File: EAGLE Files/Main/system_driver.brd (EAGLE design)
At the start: 59.4 x 64.8 mm, 12 parts

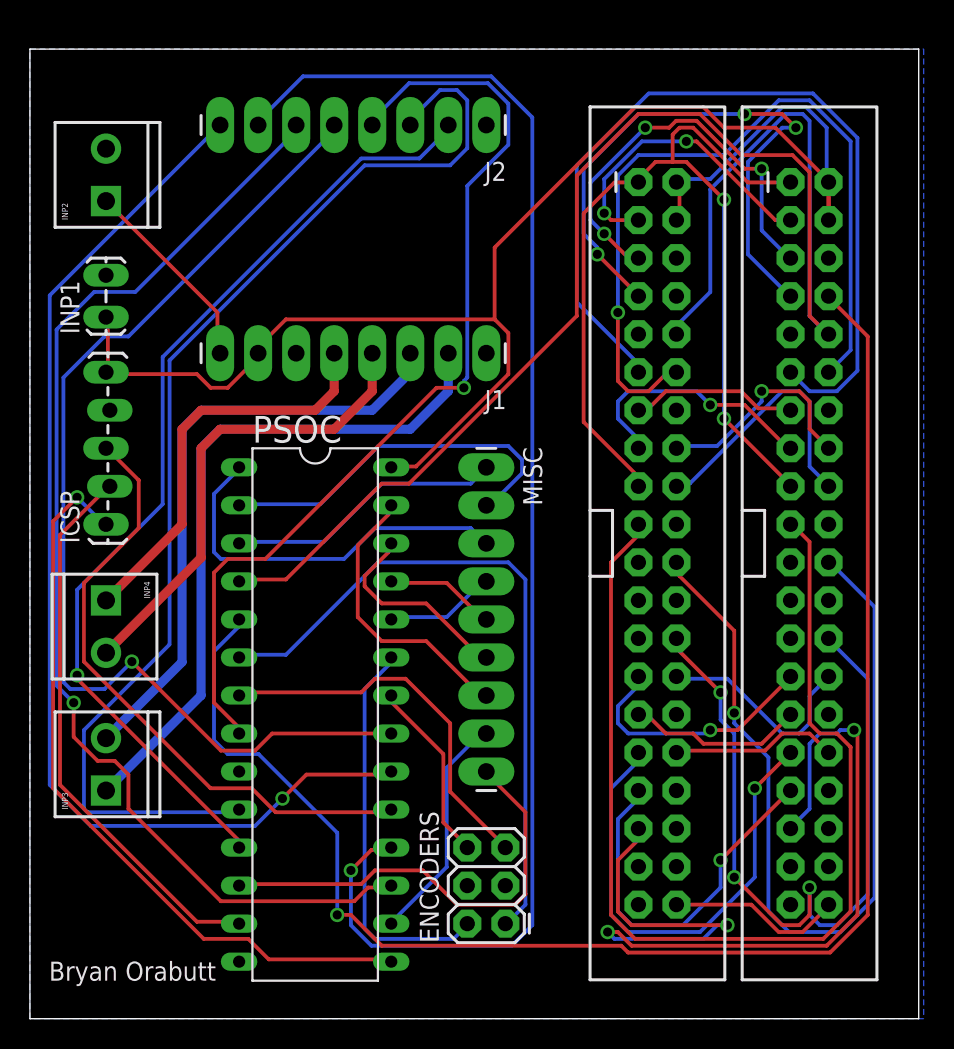
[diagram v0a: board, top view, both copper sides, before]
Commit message: updated EAGLE files
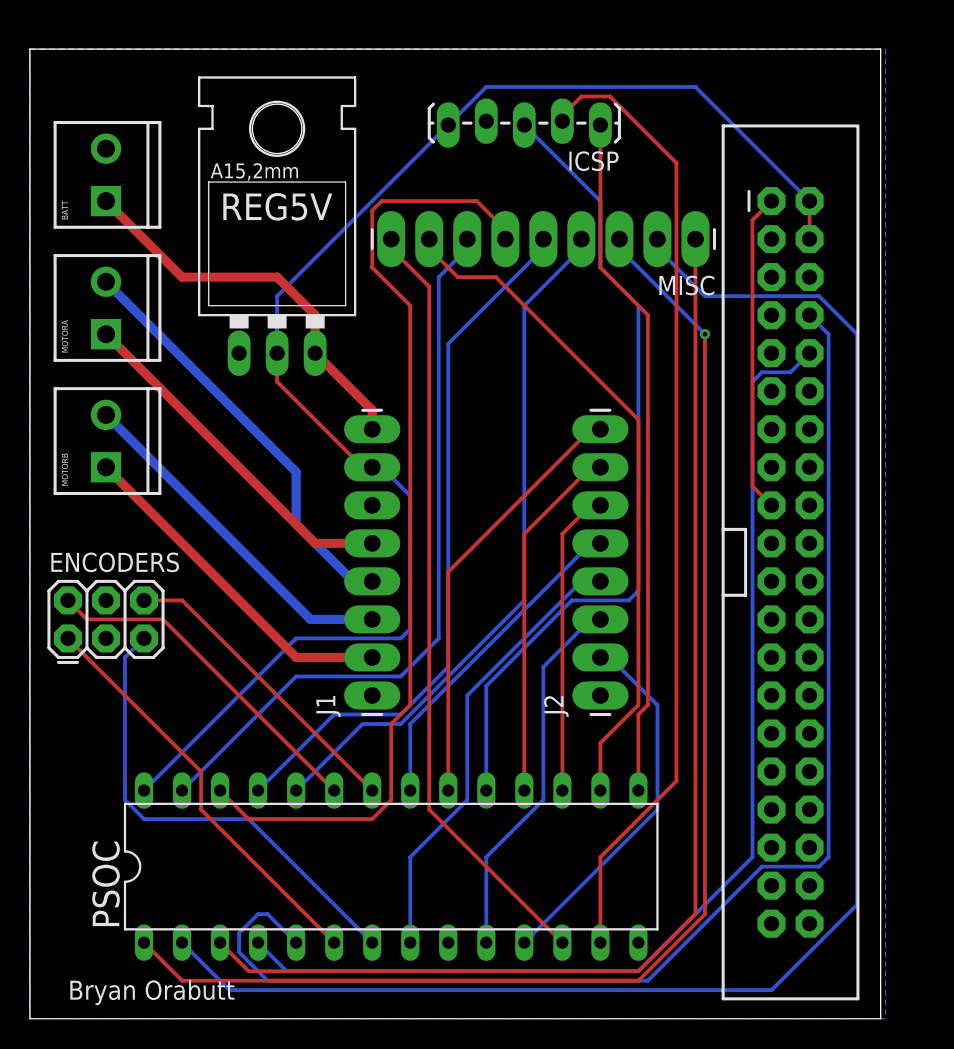
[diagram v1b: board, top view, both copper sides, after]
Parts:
- removed INP1: (no value), SparkFun-Connectors:1X02_LOCK_LONGPADS
- removed INP3, INP4: (no value), SparkFun-Connectors:SCREWTERMINAL-3.5MM-2
- removed PI1: RASPBERRYPI-40-PIN-GPIO, SparkFun-Boards:2X20-SHROUDED
- added MOTORA, MOTORB: (no value), SparkFun-Connectors:SCREWTERMINAL-3.5MM-2
- added REG5V: L7805, SparkFun-PowerIC:78XXL
- ENCODERS: value FEMALE 2x3 -> (none)
- moved ICSP 42.4 mm to (43.2, 74.9), turned to 180 degrees
- moved J2 38.9 mm to (43.2, 36.8), turned to 90 degrees
- moved ENCODERS 34.9 mm to (7.62, 40.6), turned to 0 degrees
- moved J1 24.1 mm to (27.9, 36.8), turned to 90 degrees
- moved MISC 20.7 mm to (49.5, 67.3), turned to 180 degrees
- moved PSOC 11.4 mm to (29.2, 25.4), turned to 0 degrees
- moved PI 8.98 mm to (55.9, 45.7)
- renumbered INP2 to BATT
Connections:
- net 3.3V: no longer PI1.1, PI1.17
- net AO1: now also MOTORA.1; no longer INP4.1
- net AO2: now also MOTORA.2; no longer INP4.2
- net BO1: now also MOTORB.1; no longer INP3.1
- net BO2: now also MOTORB.2; no longer INP3.2
- net CE0: no longer PI1.24
- net CE1: no longer PI1.26
- net GND: now also REG5V.IN; no longer INP1.2, PI1.14, PI1.20, PI1.25, PI1.30, PI1.34, PI1.39, PI1.6, PI1.9
- net GP12: no longer PI1.32
- net GP13: no longer PI1.33
- net GP16: no longer PI1.36
- net GP17: no longer PI1.11
- net GP18: no longer PI1.12
- net GP19: no longer PI1.35
- net GP20: no longer PI1.38
- net GP21: no longer PI1.40
- net GP22: no longer PI1.15
- net GP23: no longer PI1.16
- net GP24: no longer PI1.18
- net GP25: no longer PI1.22
- net GP26: no longer PI1.37
- net GP27: no longer PI1.13
- net GP4: no longer PI1.7
- net GP5: no longer PI1.29
- net GP6: no longer PI1.31
- net ID_SC: no longer PI1.28
- net ID_SD: no longer PI1.27
- net MISO: no longer PI1.21
- net MOSI: no longer PI1.19
- net PI_SCL: no longer PI1.5
- net PI_SDA: no longer PI1.3
- net RX: no longer PI1.8
- net SCLK: no longer PI1.23
- net TX: no longer PI1.10
- net V+: now also REG5V.OUT
- net VCC: now also REG5V.GND; no longer INP1.1, PI1.2, PI1.4
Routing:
- net MISC1: track 25.2 -> 103.2 mm
- net MOSI: track 72.5 -> 0.00 mm
- net AIN2: track 95.4 -> 24.1 mm, vias 1 -> 0
- net GP19: track 62.3 -> 0.00 mm, vias 3 -> 0
- net MISC2: track 26.0 -> 87.8 mm, vias 0 -> 1
- net MISC0: track 18.6 -> 79.2 mm
- net GP17: track 58.6 -> 0.00 mm
- net GP25: track 58.3 -> 0.00 mm, vias 1 -> 0
- net AIN1: track 77.1 -> 20.5 mm, vias 1 -> 0
- net GP18: track 53.3 -> 0.00 mm, vias 1 -> 0
- net BIN2: track 77.2 -> 25.1 mm
- net CE1: track 51.0 -> 0.00 mm, vias 3 -> 0
- net MISC5: track 13.7 -> 64.3 mm
- net STDBY: track 71.6 -> 22.1 mm, vias 1 -> 0
- net PWMA: track 74.2 -> 28.7 mm, vias 1 -> 0
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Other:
- board size 59.4 x 64.8 mm -> 56.8 x 64.8 mm

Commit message: Updated PCB files, added PSoC code
Up to date PCB and schematic files for Robot 2's driver control board.
Also added the PSoC code files and project.
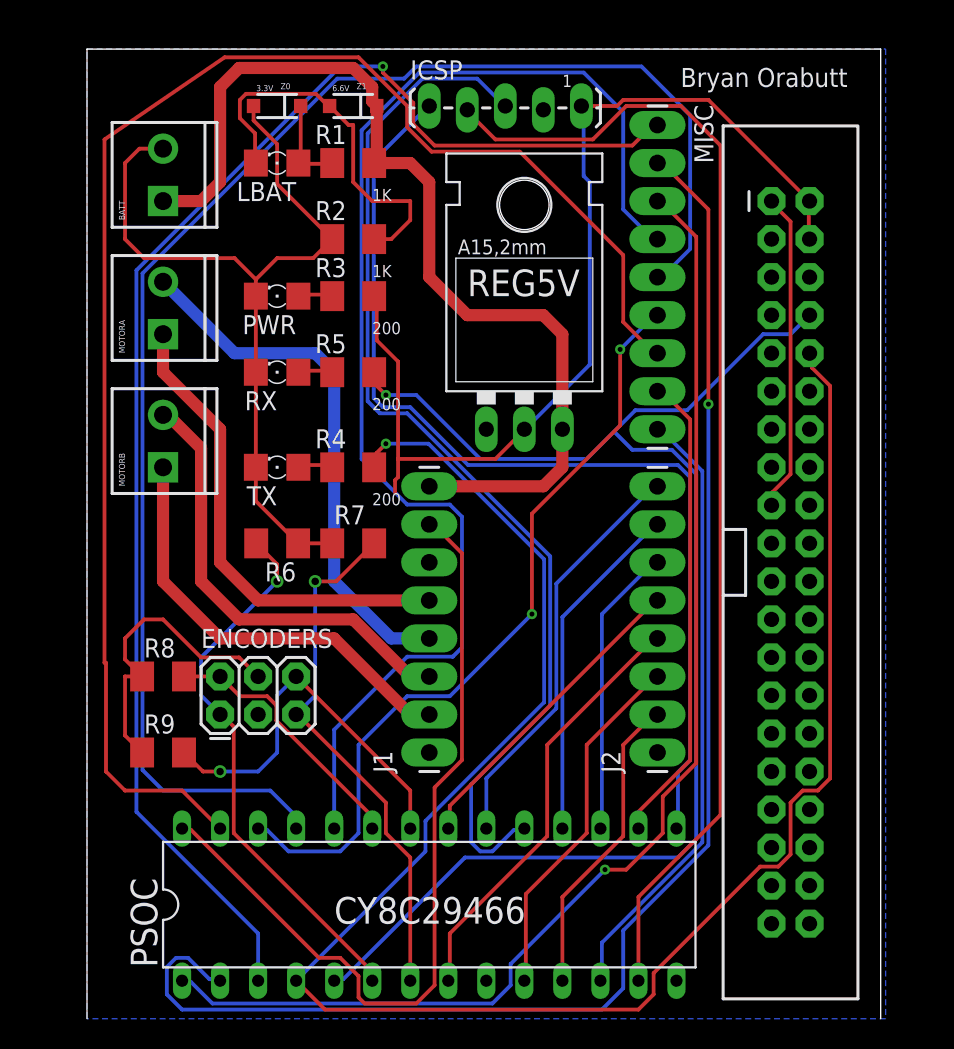
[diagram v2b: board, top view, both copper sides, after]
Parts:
- added LBAT, PWR, RX, TX: (no value), SparkFun-LED:FKIT-LED-1206
- added R1, R2: 1K, resistor:M1206
- added R3, R4, R5: 200, resistor:M1206
- added R6, R7, R8, R9: 10K, resistor:M1206
- added Z0: 3.3V, SparkFun-DiscreteSemi:SOD-123
- added Z1: 6.6V, SparkFun-DiscreteSemi:SOD-123
- moved REG5V 17.3 mm to (38.1, 58.4)
- moved ICSP 11.5 mm to (31.8, 76.2), turned to 0 degrees
- moved ENCODERS 11.4 mm to (17.8, 35.6)
- moved MISC 8.03 mm to (47.0, 74.9), turned to 270 degrees
- moved J2 5.39 mm to (47.0, 33.0)
- moved J1 5.39 mm to (31.8, 33.0)
- moved BATT 3.81 mm to (14.0, 69.8)
- moved MOTORA 3.81 mm to (14.0, 61.0)
- moved MOTORB 3.81 mm to (14.0, 52.1)
- moved PSOC 3.59 mm to (31.8, 22.9)
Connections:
- new net N$1: LBAT.A, R1.1, Z0.C
- new net N$2: LBAT.C, R2.2, Z1.A
- new net N$3: PWR.A, R3.1
- new net N$4: R4.1, TX.A
- new net N$5: R5.1, RX.A
- net ENC1A: now also R8.2
- net ENC1B: now also R9.2
- net ENC2A: now also R6.2
- net ENC2B: now also R7.2
- net GND: now also PSOC.9, PWR.C, R2.1, R6.1, R7.1, R8.1, R9.1, RX.C, TX.C, Z0.A
- net RX: now also R5.2
- net TX: now also R4.2
- net V+: now also R1.2, Z1.C
- net VCC: now also R3.2
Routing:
- net GND: track 0.00 -> 76.9 mm
- net MISC4: track 47.3 -> 101.2 mm
- net MISC6: track 48.8 -> 102.0 mm
- net TX: track 73.3 -> 125.4 mm, vias 0 -> 1
- net V+: track 26.3 -> 66.5 mm
- net MISC3: track 46.2 -> 86.2 mm
- net VCC: track 95.9 -> 123.5 mm
- net N$2: track 0.00 -> 25.6 mm
- net PSDA: track 46.0 -> 68.2 mm
- net XRES: track 54.0 -> 71.6 mm
- net MISC0: track 79.2 -> 95.1 mm, vias 0 -> 1
- net PSCK: track 64.5 -> 77.9 mm
- net MISC7: track 45.2 -> 31.9 mm
- net MISC5: track 64.3 -> 52.7 mm, vias 0 -> 2
- net MISC8: track 51.7 -> 41.0 mm
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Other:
- board size 56.8 x 64.8 mm -> 53 x 64.8 mm
- board text added: "1"
- board text added: "CY8C29466"
- board text added: "P00"
- board text added: "P02"
- board text added: "P03"
- board text added: "P04"
- board text added: "P05"
- board text added: "P06"
- board text added: "P07"
- board text added: "P12"
- board text added: "P13"

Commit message: fixed merge issues?
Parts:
- added PWR_SW: (no value), SparkFun-Electromechanical:SWITCH-SPDT
- moved Z0 1.27 mm to (21.6, 74.9)
- moved Z1 1.27 mm to (26.7, 74.9)
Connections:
- removed net MISO: PI.21
- removed net SCLK: PI.23
- new net REGIN: J1.8, PWR_SW.2, R1.2, REG5V.OUT, Z1.C
- net GND: now also PWR_SW.3
- net V+: now also PWR_SW.1; no longer J1.8, R1.2, REG5V.OUT, Z1.C
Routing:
- net REGIN: track 0.00 -> 60.3 mm, vias 0 -> 4
- net V+: track 66.5 -> 11.2 mm
- net GND: track 76.9 -> 69.9 mm
- net MISC6: track 102.0 -> 105.7 mm
- net N$1: track 6.16 -> 4.76 mm
- net N$2: track 25.6 -> 24.4 mm
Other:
- board size 53 x 64.8 mm -> 53 x 66 mm
